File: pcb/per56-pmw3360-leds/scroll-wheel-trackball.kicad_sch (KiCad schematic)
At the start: 19 parts, among them IC2 AP7335-WG-7, J2 Conn_01x06_Female, SW1 RotaryEncoder, U1 PMW3360DM-T2QU

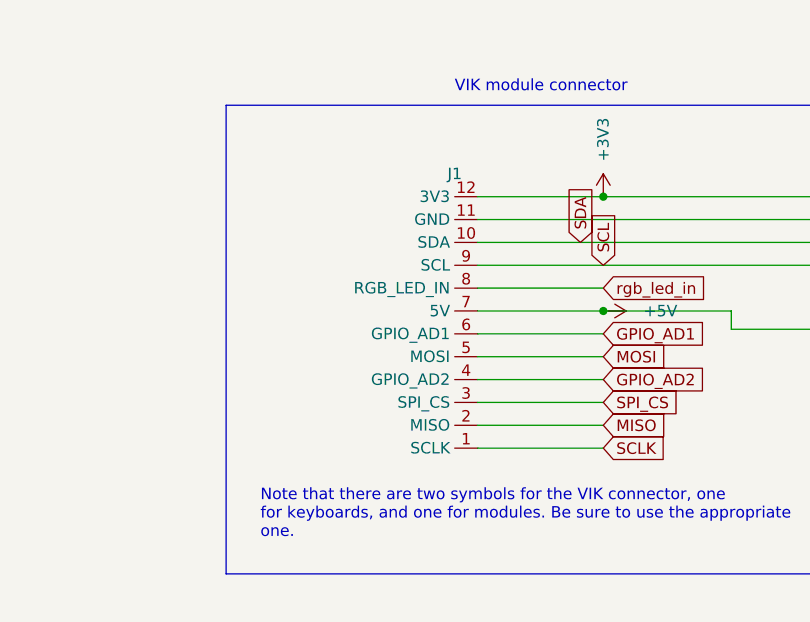
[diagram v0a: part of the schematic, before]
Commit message: updated vikm connector symbols, per some recommendations from sigprof in fingerpunch discord
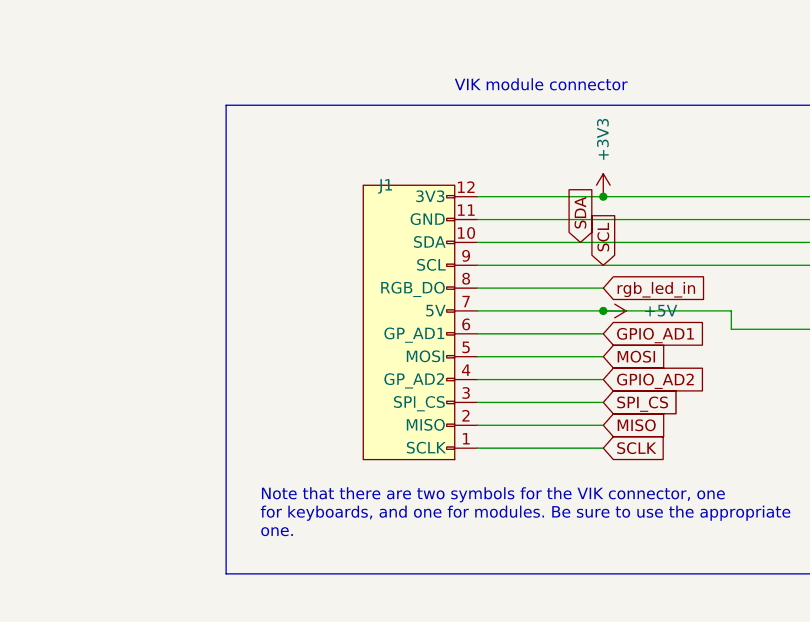
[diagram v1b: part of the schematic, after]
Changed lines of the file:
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@@
     )
   )
-  (symbol (lib_id "vik:vik-module-connector") (at 81.28 73.66 180) (unit 1)
+  (symbol (lib_id "vik:vik-module-connector") (at 73.66 74.93 180) (unit 1)
     (in_bom yes) (on_board yes) (dnp no) (fields_autoplaced)
-    (property "Reference" "J1" (at 78.74 57.15 0)
+    (property "Reference" "J1" (at 71.12 58.42 0)
       (effects (font (size 1.27 1.27)))
     )
-    (property "Value" "~" (at 81.28 80.01 0)
+    (property "Value" "~" (at 73.66 81.28 0)
       (effects (font (size 1.27 1.27)))
     )
-    (property "Footprint" "vik:vik-module-connector-horizontal" (at 81.28 80.01 0)
+    (property "Footprint" "vik:vik-module-connector-horizontal" (at 73.66 81.28 0)
       (effects (font (size 1.27 1.27)) hide)
     )
-    (property "Datasheet" "" (at 81.28 80.01 0)
+    (property "Datasheet" "" (at 73.66 81.28 0)
       (effects (font (size 1.27 1.27)) hide)
     )
-    (property "LCSC" "C479750" (at 81.28 73.66 0)
+    (property "LCSC" "C479750" (at 73.66 74.93 0)
       (effects (font (size 1.27 1.27)) hide)
     )
